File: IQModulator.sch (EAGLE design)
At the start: 122 parts, among them IC1 LM340S, IC2 OP470D, IC3 4539D, IC5 FT232RL-FULLSSOP, IC6 74AC74D, IC7 SI5351A_DEVICE_SMD, IC8 MEGA8-AI, Q1 16MHz, Q2 25MHz, X1 KLBR4

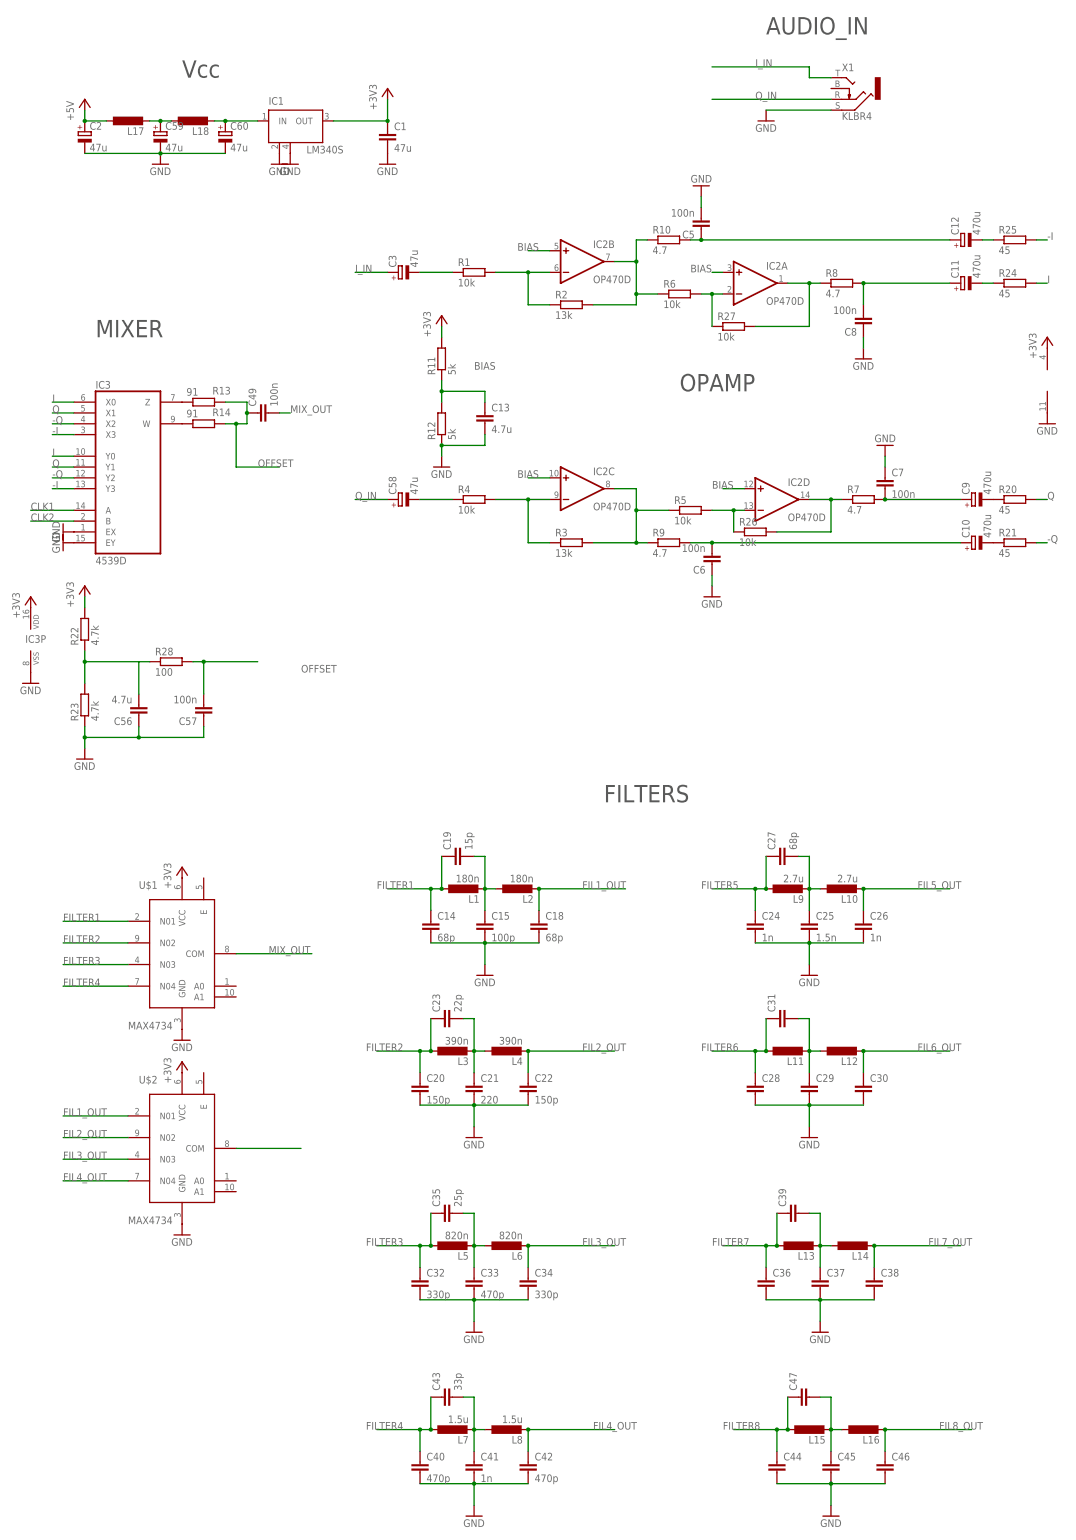
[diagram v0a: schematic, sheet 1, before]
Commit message: Filter + Lib
All Filters designed+ Eagle Lib extended
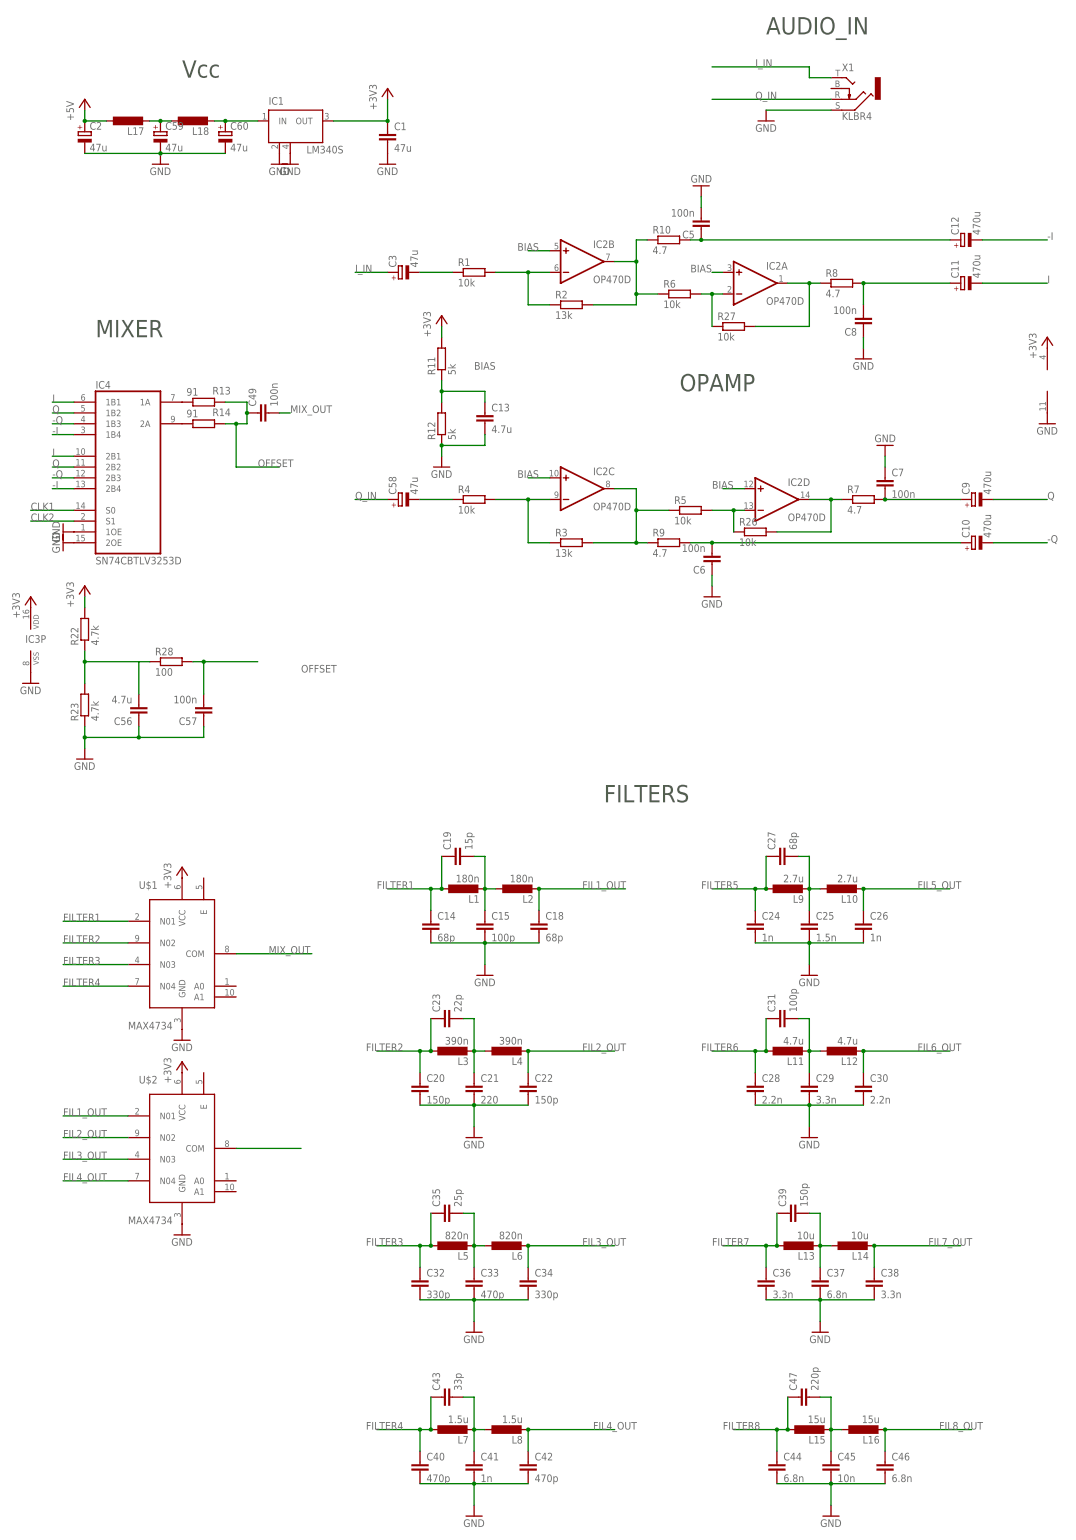
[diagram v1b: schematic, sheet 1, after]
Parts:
- removed R20, R21, R24, R25: 45, resistor:R-EU_R0805
- added IC4: SN74CBTLV3253D, _Bachelor-IQModulator:SN74CBTLV3253D
- C28, C30: value (none) -> 2.2n
- C29, C36, C38: value (none) -> 3.3n
- C31: value (none) -> 100p
- C37, C44, C46: value (none) -> 6.8n
- C39: value (none) -> 150p
- C45: value (none) -> 10n
- C47: value (none) -> 220p
- L11, L12: value (none) -> 4.7u
- L13, L14: value (none) -> 10u
- L15, L16: value (none) -> 15u
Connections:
- removed net N$24: C9.-, R20.1
- removed net N$25: C10.-, R21.1
- removed net N$38: C12.-, R25.1
- removed net N$40: C11.-, R24.1
- net -I: now also C12.-, IC41.1B4, IC41.2B4; no longer IC3A.X3, IC3A.Y3, R25.2
- net -Q: now also C10.-, IC41.1B3, IC41.2B3; no longer IC3A.X2, IC3A.Y2, R21.2
- net CLK1: now also IC41.S0; no longer IC3A.A
- net CLK2: now also IC41.S1; no longer IC3A.B
- net GND: now also IC41.1OE, IC41.2OE; no longer IC3A.EX, IC3A.EY
- net I: now also C11.-, IC41.1B1, IC41.2B1; no longer IC3A.X0, IC3A.Y0, R24.2
- net N$16: now also IC41.1A; no longer IC3A.Z
- net N$17: now also IC41.2A; no longer IC3A.W
- net Q: now also C9.-, IC41.1B2, IC41.2B2; no longer IC3A.X1, IC3A.Y1, R20.2

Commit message: PA+ Relais
Added last changes in the main schematic
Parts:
- removed C49: 100n, resistor:C-EUC0805
- removed IC3: 4539D, 45xx:4539D
- added C61: 100n, resistor:C-EUC0805
- added C62: 4.7u, resistor:C-EUC0805
- added C63: 100n, _Bachelor-IQModulator:C-EUC0805
- added D1, D2, D3, D4, D5, D6, D7, D8: (no value), diode:DIODE-DO214AA
- added L19, L20, L22: 10u, _Bachelor-IQModulator:LL0805
- added L21: 30n, _Bachelor-IQModulator:LL0805
- added R17, R18: 100, resistor:R-EU_R0805
- added R20, R21, R25: 5, _Bachelor-IQModulator:R-EU_R0805
- added R24: 0.5, _Bachelor-IQModulator:R-EU_R0805
- added R29: 120, _Bachelor-IQModulator:R-EU_R0805
- added R30: 90, _Bachelor-IQModulator:R-EU_R0805
- added T1, T2, T3, T4, T5, T6, T7, T8: (no value), zetex:NMOSSOT23
- added U$10, U$11, U$12, U$13, U$14, U$15, U$16, U$3, U$4, U$5, U$6, U$7, U$8, U$9: REED_REL, _Bachelor-IQModulator:REED_REL
- added U$17, U$18, U$19: NESG260234, _Bachelor-IQModulator:NESG260234
- added U$20, U$21: TRAFO_MID_ZAPF, _Bachelor-IQModulator:TRAFO_MID_ZAPF
- added U$22: RS_BNC_PCB, _Bachelor-IQModulator:RS_BNC_PCB
- C1: value 47u -> 1u; device resistor:C-EUC0805 -> _Bachelor-IQModulator:C-EUC0805
- C13: value 4.7u -> 1u
- C2: value 47u -> 100n; device resistor:CPOL-EUC -> _Bachelor-IQModulator:C-EUC0805
- IC1: value LM340S -> LP2992; device linear:LM340S -> _Bachelor-IQModulator:LP2992
- L1, L10, L11, L12, L13, L14, L2, L3, L4, L5, L6, L7, L8, L9: device _Bachelor_IQ_Mischer:L1008 -> _Bachelor-IQModulator:LL0805
- L17: value (none) -> 30n; device _Bachelor_IQ_Mischer:L1008 -> _Bachelor-IQModulator:LL0805
- L18: value (none) -> 10u
- R11, R12: value 5k -> 0.5; device resistor:R-EU_R0805 -> _Bachelor-IQModulator:R-EU_R0805
- R2, R3: value 13k -> 15k
- U$1, U$2: value MAX4734 -> REED_REL; device _Bachelor_IQ_Mischer:MAX4734 -> _Bachelor-IQModulator:REED_REL
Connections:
- removed net MIX_OUT: C49.2, U$1.COM
- removed net N$42: C4.2, JP2.1
- removed net N$45: C60.+, IC1.IN, L18.2
- new net CONTROL1: IC8.PD2(INT0), T1.G
- new net CONTROL2: IC8.PD3(INT1), T2.G
- new net CONTROL3: IC8.PD4(XCK/T0), T3.G
- new net CONTROL4: IC8.PD5(T1), T4.G
- new net CONTROL5: IC8.PD6(AIN0), T5.G
- new net CONTROL6: IC8.PD7(AIN1), T6.G
- new net CONTROL7: IC8.PB0(ICP), T7.G
- new net CONTROL8: IC8.PB1(OC1A), T8.G
- new net N$24: D1.C, T1.S, U$1.C+, U$9.C-
- new net N$25: C4.2, JP2.2
- new net N$38: D2.C, T2.S, U$10.C-, U$2.C+
- new net N$40: D4.C, T4.S, U$12.C-, U$4.C+
- new net N$46: D3.C, T3.S, U$11.C-, U$3.C+
- new net N$48: D5.C, T5.S, U$13.C-, U$5.C+
- new net N$50: D6.C, T6.S, U$14.C-, U$6.C+
- new net N$52: D7.C, T7.S, U$15.C-, U$7.C+
- new net N$54: D8.C, T8.S, U$16.C-, U$8.C+
- new net N$56: R12.2, U$18.E
- new net N$57: U$17.C, U$21.SEC_TOP
- new net N$58: U$18.C, U$21.SEC_BOT
- new net N$59: R21.1, R30.2, U$17.B
- new net N$60: R20.1, R30.1, U$18.B
- new net N$61: R24.2, U$19.E
- new net N$62: R25.1, U$19.B
- new net N$63: C2.1, R25.2, R29.2, U$19.C, U$20.SEC_MID
- new net N$64: L21.2, R20.2
- new net N$65: L17.2, R21.2
- new net N$66: L21.1, U$20.SEC_TOP
- new net N$67: L17.1, U$20.SEC_BOT
- new net N$68: C1.1, L22.1, U$21.SEC_MID
- new net N$69: C60.+, IC1.IN, IC1.ON/OFF, L18.2
- new net PA_IN: R13.1, R14.1, U$20.PRIM_TOP
- new net PA_OUT: U$1.IN, U$2.IN, U$21.PRIM_TOP, U$22.1, U$3.IN, U$4.IN, U$5.IN, U$6.IN, U$7.IN, U$8.IN
- net +3V3: now also C13.2, C55.1, C62.1, IC4P.VDD, L19.1, L20.1, L22.2, R29.1; no longer C1.1, C16.1, C17.2, IC3P.VDD, IC7.VDD, IC7.VDD0, R11.2, U$1.VCC, U$2.VCC
- net +5V: now also C59.+, IC5.VCCIO, L18.1, T1.D, T2.D, T3.D, T4.D, T5.D, T6.D, T7.D, T8.D; no longer C2.+, L17.1
- net BIAS: now also C61.2, R18.2; no longer C13.1, R11.1, R12.2
- net CLK1: now also IC41.S1; no longer IC41.S0
- net CLK2: now also IC41.S0; no longer IC41.S1
- net DTR: now also IC5.DTR; no longer C55.1
- net FIL1_OUT: now also U$9.IN; no longer U$2.N01
- net FIL2_OUT: now also U$10.IN; no longer U$2.N02
- net FIL3_OUT: now also U$11.IN; no longer U$2.N03
- net FIL4_OUT: now also U$12.IN; no longer U$2.N04
- net FIL5_OUT: now also U$13.IN
- net FIL6_OUT: now also U$14.IN
- net FIL7_OUT: now also U$15.IN
- net FIL8_OUT: now also U$16.IN
- net FILTER1: now also U$1.OUT; no longer U$1.N01
- net FILTER2: now also U$2.OUT; no longer U$1.N02
- net FILTER3: now also U$3.OUT; no longer U$1.N03
- net FILTER4: now also U$4.OUT; no longer U$1.N04
- net FILTER5: now also U$5.OUT
- net FILTER6: now also U$6.OUT
- net FILTER7: now also U$7.OUT
- net FILTER8: now also U$8.OUT
- net GND: now also C13.1, C2.2, C55.2, C61.1, C62.2, C63.1, D1.A, D2.A, D3.A, D4.A, D5.A, D6.A, D7.A, D8.A, IC1.GND, IC4P.VSS, JP2.1, R11.1, R24.1, U$1.C-, U$10.C+, U$11.C+, U$12.C+, U$13.C+, U$14.C+, U$15.C+, U$16.C+, U$2.C-, U$21.PRIM_BOTTOM, U$22.2, U$3.C-, U$4.C-, U$5.C-, U$6.C-, U$7.C-, U$8.C-, U$9.C+, U1.GND; no longer C13.2, C2.-, C4.1, IC1.GND@1, IC1.GND@2, IC3P.VSS, U$1.GND, U$2.GND
- net I_IN: now also C3.-; no longer C3.+
- net N$1: now also C57.2, R17.1, R28.2; no longer IC5.VCCIO
- net N$2: now also C3.+; no longer C3.-
- net N$26: now also R19.1, S1.S1; no longer U1.GND
- net N$30: now also C16.1, IC7.VDD, L20.2; no longer C55.2, IC5.DTR
- net N$36: now also R18.1
- net N$39: now also C17.2, IC7.VDD0, L19.2; no longer U$2.COM
- net N$4: now also C58.+; no longer C58.-
- net N$44: now also R11.2, U$17.E; no longer C59.+, L17.2, L18.1
- net OFFSET: now also C63.2, R17.2, U$20.PRIM_BOTTOM; no longer C49.1, C57.2, R13.1, R14.1, R28.2
- net Q_IN: now also C58.-; no longer C58.+
- net RESET: now also C4.1; no longer JP2.2

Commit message: Beta V. 0.1
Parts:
- removed U1: (no value), MicroUSB:USB""
- added C49: 1u, resistor:C-EUC0805
- added C64: 100n, resistor:C-EUC0805
- added C65: 10n, resistor:C-EUC0805
- added C66, C67: 1p, _Bachelor-IQModulator:C-EUC0805
- added K1: (no value), Input-Output_Connectors_rev15d:629105150521
- C53: value 0.1u -> 100n
- R17: value 100 -> 500
- X2: value (none) -> CLK2
- renumbered X3 to CLK3
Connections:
- new net LOAD: U$10.OUT, U$11.OUT, U$12.OUT, U$13.OUT, U$14.OUT, U$15.OUT, U$16.OUT, U$22.1, U$9.OUT
- new net N$42: C65.1, IC1.BYPASS
- net +3V3: now also C49.1, C64.2
- net +5V: now also K1.1VCC; no longer U1.VBUS
- net D+: now also K1.3D+; no longer U1.D+
- net D-: now also K1.2D-; no longer U1.D-
- net GND: now also C49.2, C64.1, C65.2, K1.5GND, K1.GND@1, K1.GND@2; no longer U1.GND
- net N$57: now also C66.2
- net N$58: now also C67.1
- net N$59: now also C67.2
- net N$60: now also C66.1
- net PA_OUT: no longer U$22.1
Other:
- moved on the sheet: U$22

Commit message: Started with Layout
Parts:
- removed C61: 100n, resistor:C-EUC0805
- removed L20: 10u, _Bachelor-IQModulator:LL0805
- removed R18: 100, resistor:R-EU_R0805
- added C68: 470u, resistor:CPOL-EUD
- added C69, C75: 100n, resistor:C-EUC0805
- added C70, C71: 1p, _Bachelor-IQModulator:C-EUC0805
- added C72, C73: 47u, resistor:CPOL-EUC
- added C74: 4.7u, resistor:C-EUC0805
- added JP3: (no value), jumper:JP2E
- added R31, R32: 4.7k, resistor:R-EU_R0805
- added R33: 100, resistor:R-EU_R0805
- IC2: value OP470D -> TLV2464CDD; device linear:OP470D -> _Bachelor-IQModulator:TLV2464CDD
- L19: device _Bachelor-IQModulator:LL0805 -> _Bachelor_IQ_Mischer:L1008
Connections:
- removed net N$24: D1.C, T1.S, U$1.C+, U$9.C-
- removed net N$50: D6.C, T6.S, U$14.C-, U$6.C+
- removed net N$52: D7.C, T7.S, U$15.C-, U$7.C+
- new net CLEAN_5V: C73.+, JP3.3, L19.2
- new net N$43: D4.A, T4.D, U$12.C+, U$4.C-
- new net N$45: D3.A, T3.D, U$11.C+, U$3.C-
- new net N$47: D2.A, T2.D, U$10.C+, U$2.C-
- new net N$49: C70.2, U$21.SEC_BOT
- new net N$51: C74.2, R31.1, R32.2, R33.1
- net +3V3: now also C16.1, C17.2, IC7.VDD, IC7.VDD0, JP3.1; no longer C64.2, IC2P.V+, L19.1, L20.1
- net +5V: now also C69.1, C72.+, D1.C, D2.C, D3.C, D4.C, D5.C, D6.C, D7.C, D8.C, L19.1, U$1.C+, U$10.C-, U$11.C-, U$12.C-, U$13.C-, U$14.C-, U$15.C-, U$16.C-, U$2.C+, U$3.C+, U$4.C+, U$5.C+, U$6.C+, U$7.C+, U$8.C+, U$9.C-; no longer T1.D, T2.D, T3.D, T4.D, T5.D, T6.D, T7.D, T8.D
- net BIAS: now also C75.2, R33.2; no longer C61.2, R18.2
- net GND: now also C68.-, C69.2, C72.-, C73.-, C74.1, C75.1, R32.1, T1.S, T2.S, T3.S, T4.S, T5.S, T6.S, T7.S, T8.S; no longer C61.1, D1.A, D2.A, D3.A, D4.A, D5.A, D6.A, D7.A, D8.A, U$1.C-, U$10.C+, U$11.C+, U$12.C+, U$13.C+, U$14.C+, U$15.C+, U$16.C+, U$2.C-, U$3.C-, U$4.C-, U$5.C-, U$6.C-, U$7.C-, U$8.C-, U$9.C+
- net N$30: now also D6.A, T6.D, U$14.C+, U$6.C-; no longer C16.1, IC7.VDD, L20.2
- net N$36: no longer R18.1
- net N$38: now also D1.A, T1.D, U$1.C-, U$9.C+; no longer D2.C, T2.S, U$10.C-, U$2.C+
- net N$39: now also D5.A, T5.D, U$13.C+, U$5.C-; no longer C17.2, IC7.VDD0, L19.2
- net N$40: now also D7.A, T7.D, U$15.C+, U$7.C-; no longer D4.C, T4.S, U$12.C-, U$4.C+
- net N$46: now also D8.A, T8.D, U$16.C+, U$8.C-; no longer D3.C, T3.S, U$11.C-, U$3.C+
- net N$48: now also C71.1, U$21.SEC_TOP; no longer D5.C, T5.S, U$13.C-, U$5.C+
- net N$54: now also C64.2, IC2P.V+, JP3.2, R31.2; no longer D8.C, T8.S, U$16.C-, U$8.C+
- net N$57: now also C71.2; no longer U$21.SEC_TOP
- net N$58: now also C70.1; no longer U$21.SEC_BOT
- net OFFSET: now also C68.+
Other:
- moved on the sheet: C64, T1, T2, T3, T4, T5, T6, T7, T8

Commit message: updated board
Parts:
- added R18: 0, resistor:R-EU_R0805
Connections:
- net GND: now also R18.1, R18.2
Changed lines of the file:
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@@
 <part name="C75" library="resistor" deviceset="C-EU" device="C0805" value="100n"/>
 <part name="GND61" library="supply1" deviceset="GND" device=""/>
+<part name="R18" library="resistor" deviceset="R-EU_" device="R0805" value="0"/>
+<part name="GND49" library="supply1" deviceset="GND" device=""/>
+<part name="GND62" library="supply1" deviceset="GND" device=""/>
 </parts>
 <sheets>
@@
 <instance part="C75" gate="G$1" x="73.66" y="-81.28" rot="R180"/>
 <instance part="GND61" gate="1" x="58.42" y="-88.9"/>
+<instance part="R18" gate="G$1" x="-43.18" y="-93.98"/>
+<instance part="GND49" gate="1" x="-50.8" y="-93.98" rot="R270"/>
+<instance part="GND62" gate="1" x="-35.56" y="-93.98" rot="R90"/>
 </instances>
 <busses>
@@
 <junction x="58.42" y="-86.36"/>
 </segment>
+<segment>
+<pinref part="R18" gate="G$1" pin="1"/>
+<pinref part="GND49" gate="1" pin="GND"/>
+</segment>
+<segment>
+<pinref part="R18" gate="G$1" pin="2"/>
+<pinref part="GND62" gate="1" pin="GND"/>
+</segment>
 </net>

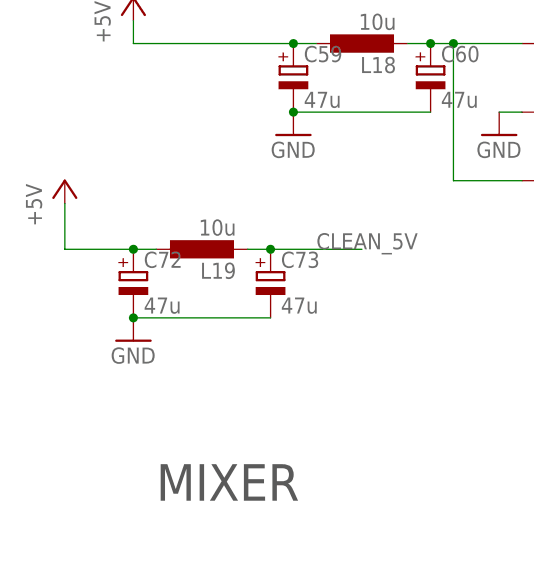
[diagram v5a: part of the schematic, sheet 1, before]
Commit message: Board smaller now!
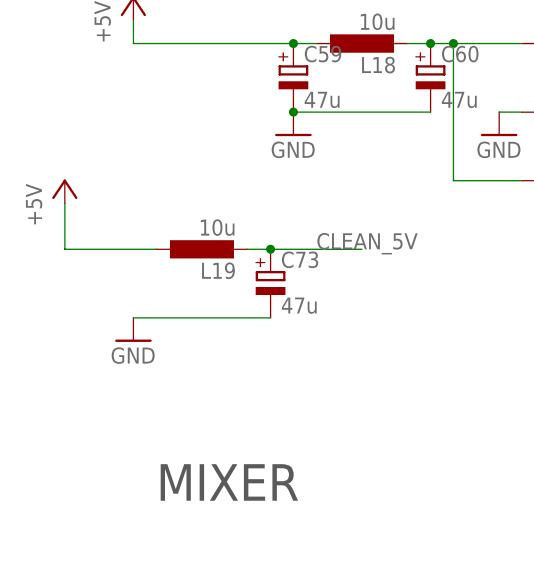
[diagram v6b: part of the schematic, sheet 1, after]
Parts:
- removed C72: 47u, resistor:CPOL-EUC
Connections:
- net +5V: no longer C72.+
- net GND: no longer C72.-
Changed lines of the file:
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@@
 <part name="L19" library="_Bachelor_IQ_Mischer" deviceset="L1008" device="" value="10u"/>
 <part name="GND60" library="supply1" deviceset="GND" device=""/>
-<part name="C72" library="resistor" deviceset="CPOL-EU" device="C" value="47u"/>
 <part name="C73" library="resistor" deviceset="CPOL-EU" device="C" value="47u"/>
 <part name="R31" library="resistor" deviceset="R-EU_" device="R0805" value="4.7k"/>
@@
 <instance part="L19" gate="&gt;NAME" x="-86.36" y="35.56" rot="R90"/>
 <instance part="GND60" gate="1" x="-93.98" y="25.4"/>
-<instance part="C72" gate="G$1" x="-93.98" y="33.02"/>
 <instance part="C73" gate="G$1" x="-78.74" y="33.02"/>
 <instance part="R31" gate="G$1" x="40.64" y="-63.5" rot="R90"/>
@@
 <wire x1="-78.74" y1="27.94" x2="-93.98" y2="27.94" width="0.1524" layer="91"/>
 <pinref part="GND60" gate="1" pin="GND"/>
-<junction x="-93.98" y="27.94"/>
-<pinref part="C72" gate="G$1" pin="-"/>
 <pinref part="C73" gate="G$1" pin="-"/>
 </segment>
@@
 <wire x1="-101.6" y1="35.56" x2="-101.6" y2="40.64" width="0.1524" layer="91"/>
 <pinref part="L19" gate="&gt;NAME" pin="1"/>
-<pinref part="C72" gate="G$1" pin="+"/>
-<wire x1="-93.98" y1="35.56" x2="-91.44" y2="35.56" width="0.1524" layer="91"/>
-<wire x1="-101.6" y1="35.56" x2="-93.98" y2="35.56" width="0.1524" layer="91"/>
-<junction x="-93.98" y="35.56"/>
-</segment>
-</net>
+<wire x1="-101.6" y1="35.56" x2="-91.44" y2="35.56" width="0.1524" layer="91"/>
+</segment>
+</net>
